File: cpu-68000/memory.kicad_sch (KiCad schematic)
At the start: 14 parts, among them U401 IS61C5128AL-10TLI, U402 IS61C5128AL-10TLI, U403 IS61C5128AL-10TLI, U404 IS61C5128AL-10TLI

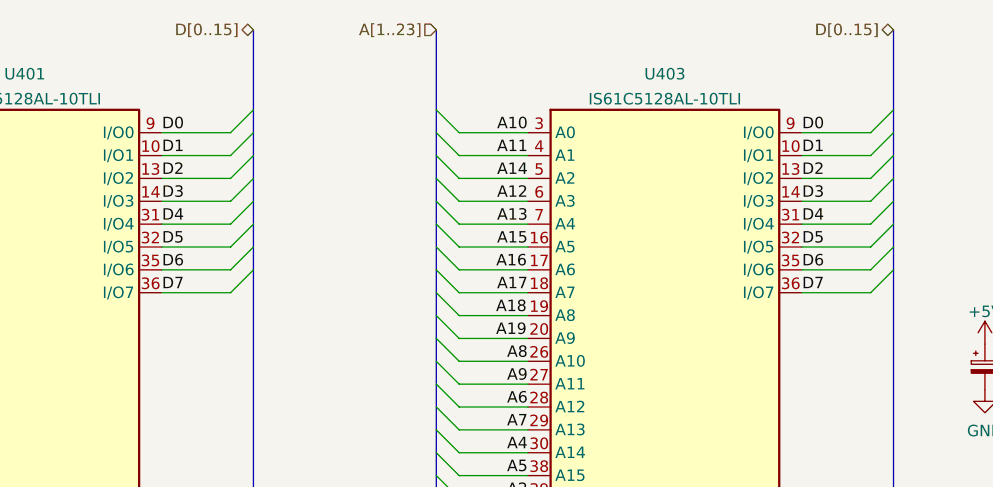
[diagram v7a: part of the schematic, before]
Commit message: Start peripheral routing
- Begin routing some of the peripheral section, particularly the NVRAM
  is fully connected (sans chip select) now

- Added an I2C EEPROM (with serial number) on board the CPU card for
  automatic identification

- Minor cleanups and space squishing of the board. There may in fact be
  sufficient space to still fit a boot ROM (likely a surface mount
  flash, maybe PLCC; probably not two full DIP sockets)
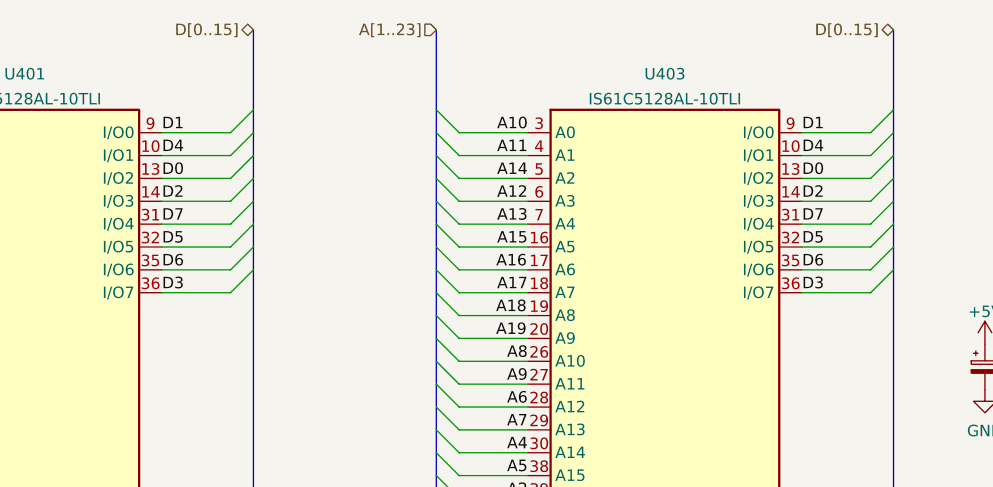
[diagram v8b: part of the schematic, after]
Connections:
- net D0: now also U401.13 (I/O2), U403.13 (I/O2); no longer U401.9 (I/O0), U403.9 (I/O0)
- net D1: now also U401.9 (I/O0), U403.9 (I/O0); no longer U401.10 (I/O1), U403.10 (I/O1)
- net D2: now also U401.14 (I/O3), U403.14 (I/O3); no longer U401.13 (I/O2), U403.13 (I/O2)
- net D3: now also U401.36 (I/O7), U403.36 (I/O7); no longer U401.14 (I/O3), U403.14 (I/O3)
- net D4: now also U401.10 (I/O1), U403.10 (I/O1); no longer U401.31 (I/O4), U403.31 (I/O4)
- net D7: now also U401.31 (I/O4), U403.31 (I/O4); no longer U401.36 (I/O7), U403.36 (I/O7)
